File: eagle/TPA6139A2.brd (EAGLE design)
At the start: 34 x 44.4 mm, 12 parts

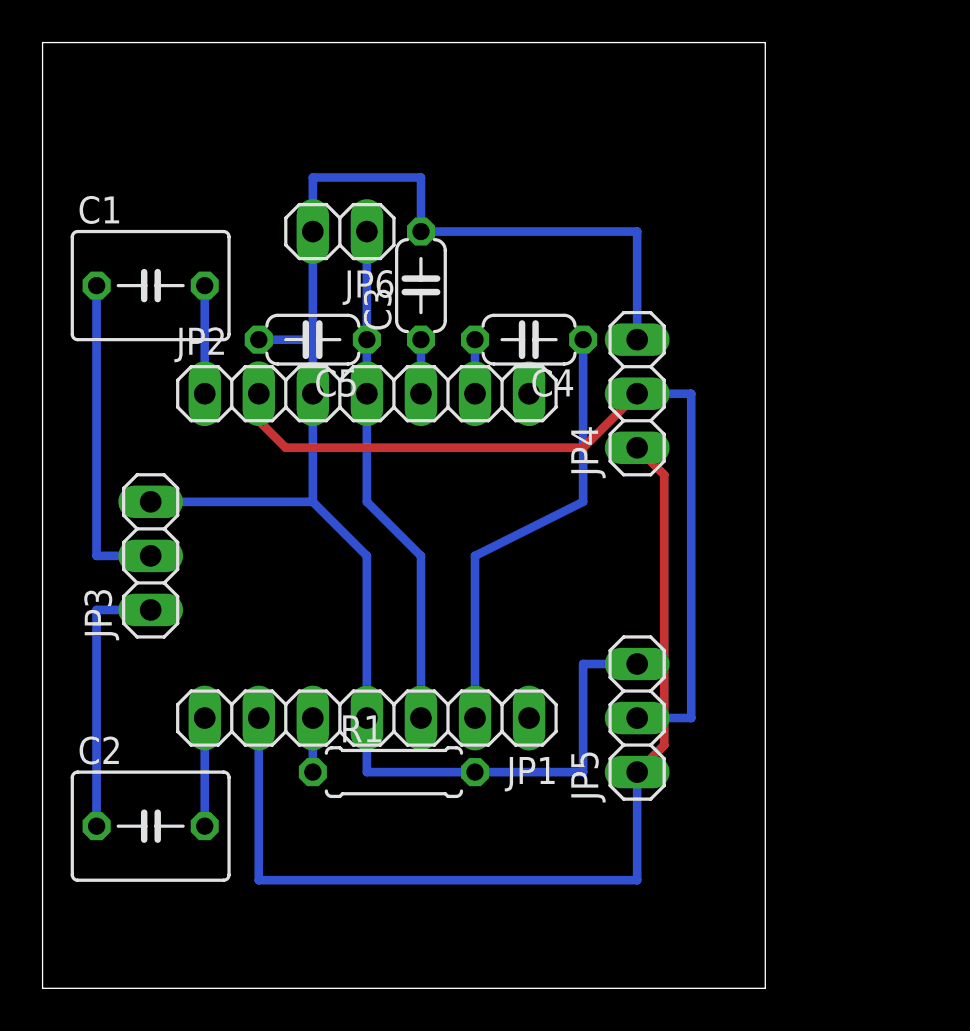
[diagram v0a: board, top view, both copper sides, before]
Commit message: 回路図、基板図修正
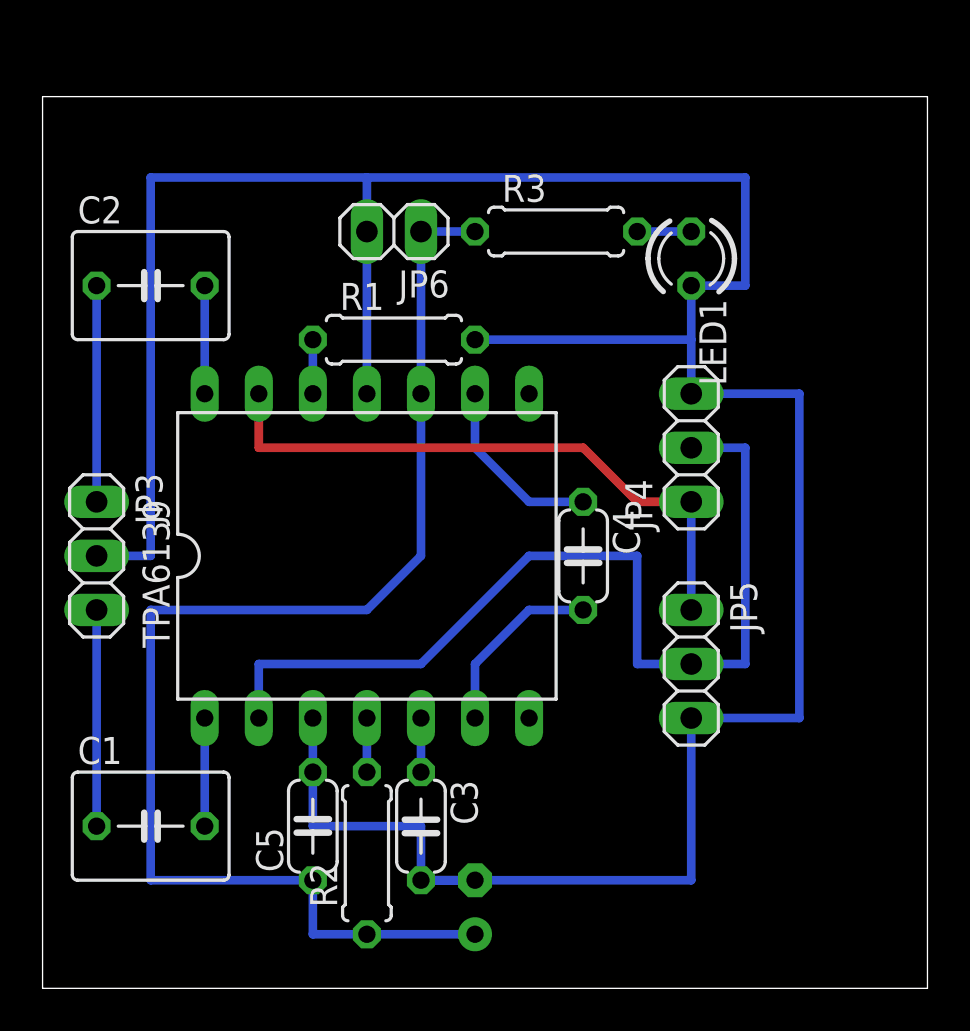
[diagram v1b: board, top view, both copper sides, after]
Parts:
- removed JP1, JP2: (no value), pinhead:1X07
- added C6: 47u, rcl:TT2D5L
- added LED1: Blue, led:LED3MM
- added R2: 10k, rcl:0207/7
- added R3: 1k, rcl:0207/7
- added TPA6139: DIL14-6, mylib:DIL14-6
- R1: value 22k -> 47k
- moved C1 25.4 mm to (5.08, 7.62)
- moved C2 25.4 mm to (5.08, 33.0)
- moved C3 25.4 mm to (17.8, 7.62), turned to 270 degrees
- moved C5 22.9 mm to (12.7, 7.62), turned to 90 degrees
- moved R1 20.3 mm to (16.5, 30.5)
- moved C4 10.5 mm to (25.4, 20.3), turned to 270 degrees
- moved JP4 3.59 mm to (30.5, 25.4)
- moved JP5 3.59 mm to (30.5, 15.2), turned to 270 degrees
- moved JP6 2.54 mm to (16.5, 35.6)
- moved JP3 2.54 mm to (2.54, 20.3), turned to 270 degrees
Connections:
- removed net N$11: JP1.5, R1.1
- new net N$3: R2.2, TPA6139.4
- new net N$4: C3.1, TPA6139.5
- new net N$5: R1.1, TPA6139.12
- net +3V3: now also C6.+, R2.1, R3.1, TPA6139.10; no longer JP1.3, JP2.4
- net AGND: now also C6.-, JP3.2, LED1.K, TPA6139.11, TPA6139.3; no longer JP1.4, JP2.3, JP3.3
- net IN-L: now also JP3.3; no longer JP3.2
- net N$1: now also TPA6139.14; no longer JP1.7
- net N$10: now also TPA6139.9; no longer JP1.2
- net N$2: now also TPA6139.1; no longer JP2.1
- net N$6: now also LED1.A, R3.2; no longer C3.1, JP2.5
- net N$9: now also TPA6139.6; no longer JP2.6
- net OUT-L: now also TPA6139.2; no longer JP2.2
- net OUT-R: now also TPA6139.13; no longer JP1.6
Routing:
- net AGND: track 79.8 -> 142.2 mm
- net +3V3: track 23.9 -> 62.0 mm
- net OUT-R: track 46.8 -> 29.0 mm
- net N$10: track 20.9 -> 8.67 mm
- net N$9: track 2.54 -> 8.67 mm
- net IN-L: track 15.2 -> 10.2 mm
- net OUT-L: track 40.9 -> 45.3 mm
- net N$5: track 0.00 -> 2.54 mm
- net N$4: track 0.00 -> 2.54 mm
- net N$3: track 0.00 -> 2.54 mm
- net N$11: track 2.54 -> 0.00 mm
- net IN-R: track 12.7 -> 10.2 mm
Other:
- board size 34 x 44.4 mm -> 41.6 x 41.9 mm
